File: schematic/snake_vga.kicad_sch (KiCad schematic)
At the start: 14 parts, among them Q1 TN2106, Q2 TN2106, U1 NUCLEO-LxxxKx, U2 UPduino_v3.1, U3 SLP120B16-16

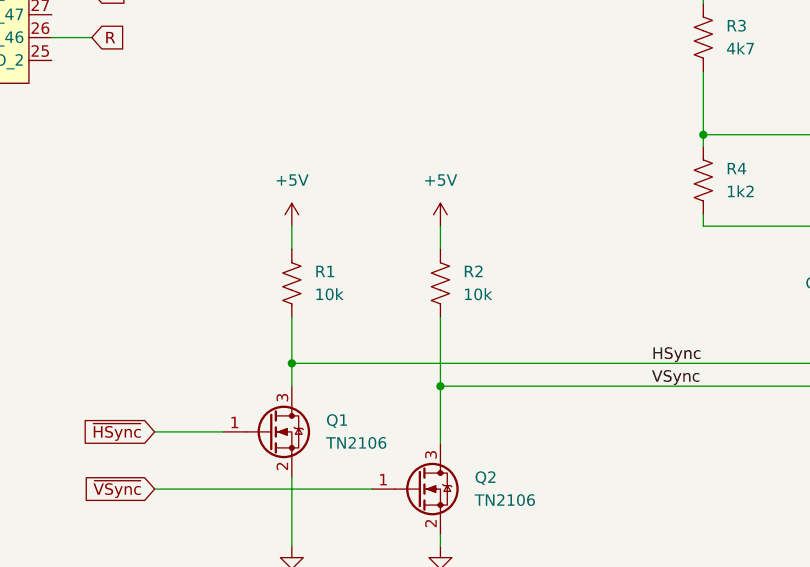
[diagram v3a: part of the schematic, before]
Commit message: changed pullup resistor value for logic level shifter
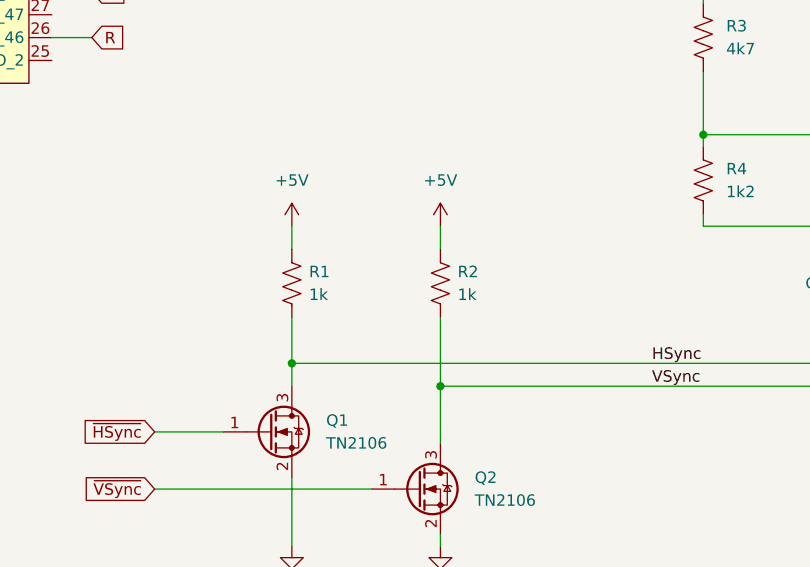
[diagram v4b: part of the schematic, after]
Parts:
- R1, R2: value 10k -> 1k
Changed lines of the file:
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@@
   (symbol (lib_id "Device:R_US") (at 130.175 132.08 0) (unit 1)
     (in_bom yes) (on_board yes) (dnp no) (fields_autoplaced)
-    (property "Reference" "R2" (at 132.715 130.81 0)
+    (property "Reference" "R2" (at 132.08 130.81 0)
       (effects (font (size 1.27 1.27)) (justify left))
     )
-    (property "Value" "10k" (at 132.715 133.35 0)
+    (property "Value" "1k" (at 132.08 133.35 0)
       (effects (font (size 1.27 1.27)) (justify left))
     )
@@
   (symbol (lib_id "Device:R_US") (at 113.665 132.08 0) (unit 1)
     (in_bom yes) (on_board yes) (dnp no) (fields_autoplaced)
-    (property "Reference" "R1" (at 116.205 130.81 0)
+    (property "Reference" "R1" (at 115.57 130.81 0)
       (effects (font (size 1.27 1.27)) (justify left))
     )
-    (property "Value" "10k" (at 116.205 133.35 0)
+    (property "Value" "1k" (at 115.57 133.35 0)
       (effects (font (size 1.27 1.27)) (justify left))
     )

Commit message: Finalized Schematic
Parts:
- removed U3: SLP120B16-16, symbol Keypad_Lib:SLP120B16-16
- added Q3, Q4, Q5: 2N3904, Package_TO_SOT_THT:TO-92_Inline, symbol Transistor_BJT:2N3904
- added R10, R11, R9: 10k, symbol Device:R_US
- added SW1, SW2, SW3, SW4: SW_Push, symbol Switch:SW_Push
- R1, R2: value 1k -> 270R
- R3, R5, R7: value 4k7 -> 1k2
- R4, R6, R8: value 1k2 -> 1k
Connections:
- net +5V: now also Q3.3 (C), Q4.3 (C), Q5.3 (C)
- net GND: now also J1.11 (ID0), J1.12 (ID1), J1.4 (ID2), R10.2, R11.2, R9.2, SW1.1, SW2.1, SW3.1, SW4.1
- net at R3.2, R4.1: now also Q5.2 (B); no longer J1.3 (Blue)
- net at R7.2, R8.1: now also Q3.2 (B); no longer J1.1 (Red)
- net at R5.2, R6.1: now also Q4.2 (B); no longer J1.2 (Green)
- net BUTTON_DOWN: now reaches U1.5 (D2/PA12)
- net BUTTON_DOWN: now also SW2.2
- net BUTTON_RIGHT: now reaches U1.6 (D3/PB0)
- net BUTTON_RIGHT: now also SW4.2
- net BUTTON_UP: now reaches U1.7 (D4/PB7)
- net BUTTON_UP: now also SW1.2
- net BUTTON_LEFT: now reaches U1.8 (D5/PB6)
- net BUTTON_LEFT: now also SW3.2
- new net: J1.1 (Red), Q3.1 (E), R9.1
- new net: J1.2 (Green), Q4.1 (E), R10.1
- new net: J1.3 (Blue), Q5.1 (E), R11.1
- no-connect marks 4 -> 0
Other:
- note added: "12/7/2023"
- note added: "VGA Connector"
- note added: "emitter follower circuit to provide impedance buffer"
- note removed: "11/15/2023"
- note removed: "keypad"
- moved on the sheet: J1, Q1, Q2, R1, R2, R3, R4, R5, R6, R7, R8, U1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
